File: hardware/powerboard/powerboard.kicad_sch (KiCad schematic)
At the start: 55 parts, among them J1 USB_B_Micro, J2 Boot Header, J3 Power Header, J4 SPI_0 Header, J5 Debug Header, J6 SPI_1 Header, J7 I2C_0 Header, J8 I2C_1 Header, SW1 Oct_Up, SW2 RESET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

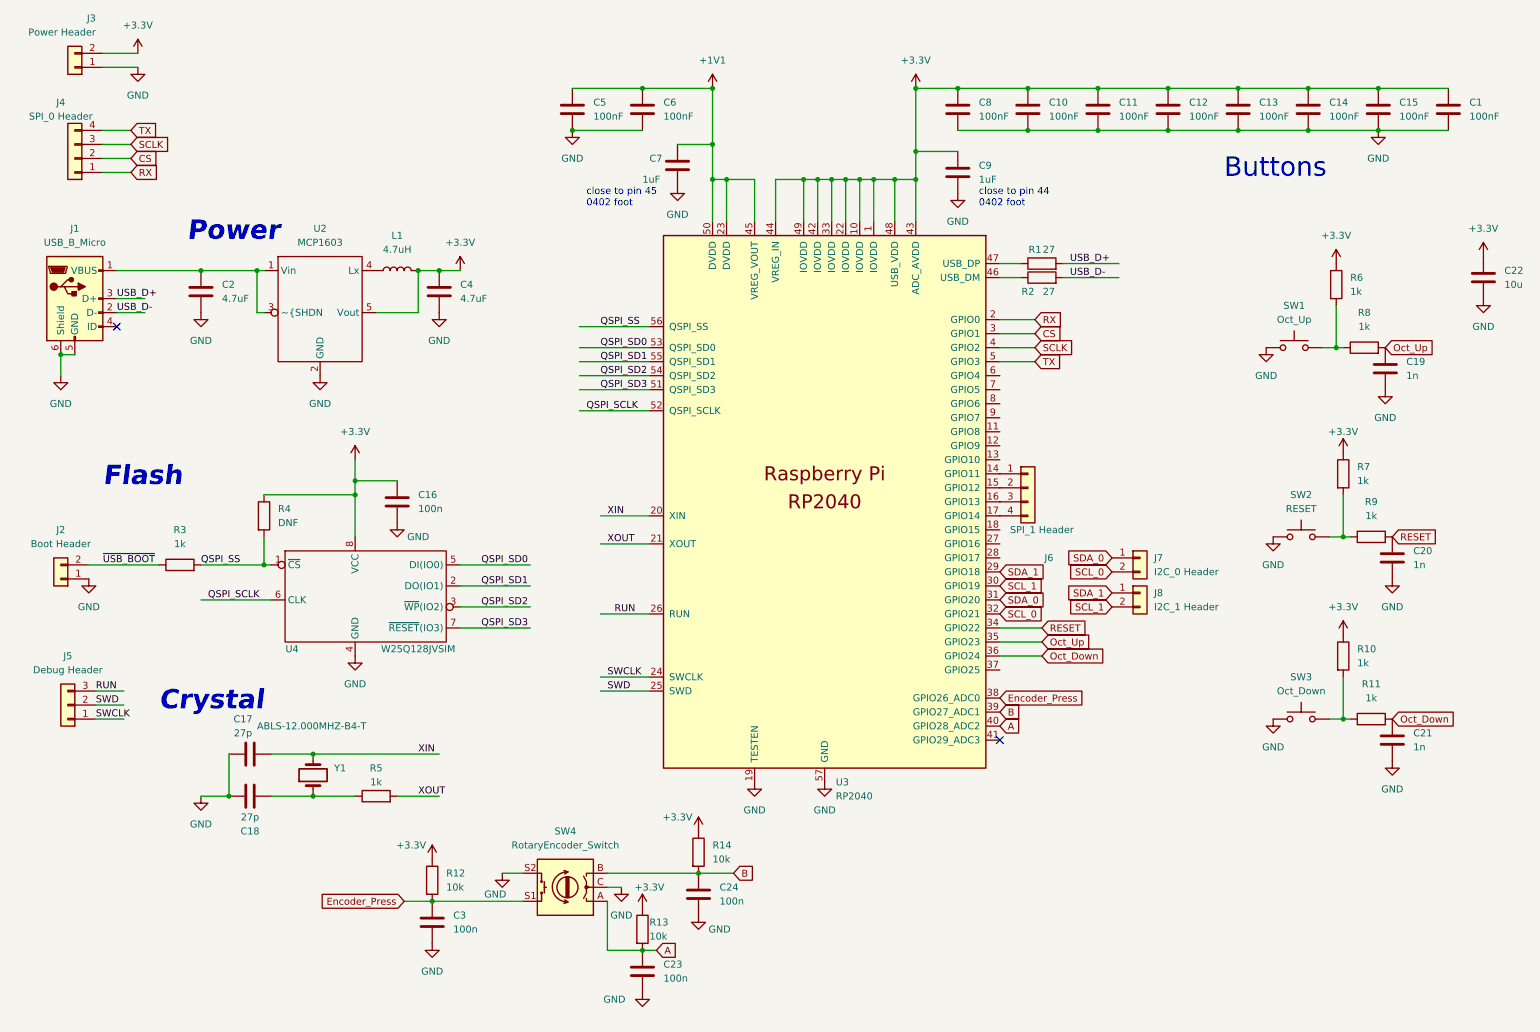
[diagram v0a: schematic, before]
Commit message: Power Board PCB: UART, LED's Smaller Crystal
Replaced Old Crystal with 3N12000G33YC
Added UART_0 with GP16 and GP17
Added 4 LED's with 330OHM Resistors on GP4-GP7
SPI Trace Widths 11.55 mil = 50Ohm Impedance
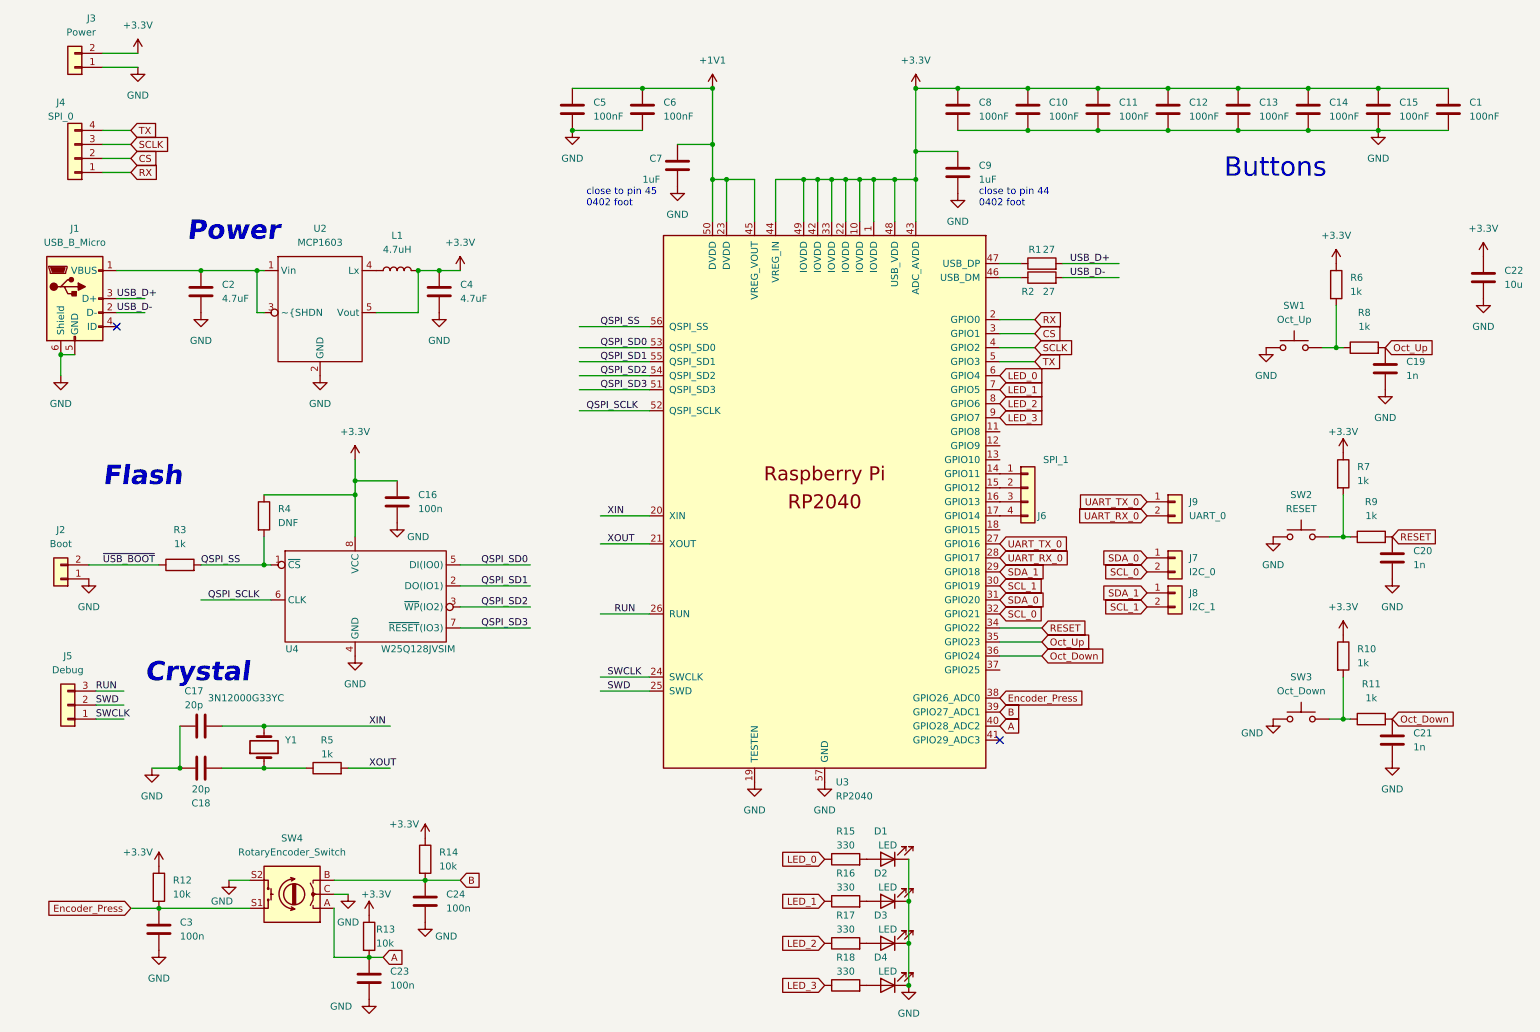
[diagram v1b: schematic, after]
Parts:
- added D1, D2, D3, D4: LED, LED_SMD:LED_0603_1608Metric, symbol Device:LED
- added J9: UART_0, Connector_PinHeader_2.54mm:PinHeader_1x02_P2.54mm_Vertical, symbol Connector_Generic:Conn_01x02
- added R15, R16, R17, R18: 330, Resistor_SMD:R_0603_1608Metric, symbol Device:R
- C17, C18: value 27p -> 20p
- J2: value Boot Header -> Boot
- J3: value Power Header -> Power
- J4: value SPI_0 Header -> SPI_0
- J5: value Debug Header -> Debug
- J6: value SPI_1 Header -> SPI_1
- J7: value I2C_0 Header -> I2C_0
- J8: value I2C_1 Header -> I2C_1
- Y1: value ABLS-12.000MHZ-B4-T -> 3N12000G33YC; footprint RP2040_minimal:Crystal_SMD_HC49-US -> Crystal:Crystal_SMD_3225-4Pin_3.2x2.5mm
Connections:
- net GND: now also D1.1 (K), D2.1 (K), D3.1 (K), D4.1 (K)
- net UART_TX_0: now reaches U3.27 (GPIO16)
- net UART_TX_0: now also J9.1 (Pin_1)
- net UART_RX_0: now reaches U3.28 (GPIO17)
- net UART_RX_0: now also J9.2 (Pin_2)
- net LED_0: now reaches U3.6 (GPIO4)
- net LED_0: now also R15.1
- net LED_1: now reaches U3.7 (GPIO5)
- net LED_1: now also R16.1
- net LED_2: now reaches U3.8 (GPIO6)
- net LED_2: now also R17.1
- net LED_3: now reaches U3.9 (GPIO7)
- net LED_3: now also R18.1
- new net: D4.2 (A), R18.2
- new net: D2.2 (A), R16.2
- new net: D3.2 (A), R17.2
- new net: D1.2 (A), R15.2
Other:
- moved on the sheet: C17, C18, C23, C24, C3, J7, J8, R12, R13, R14, R5, SW4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

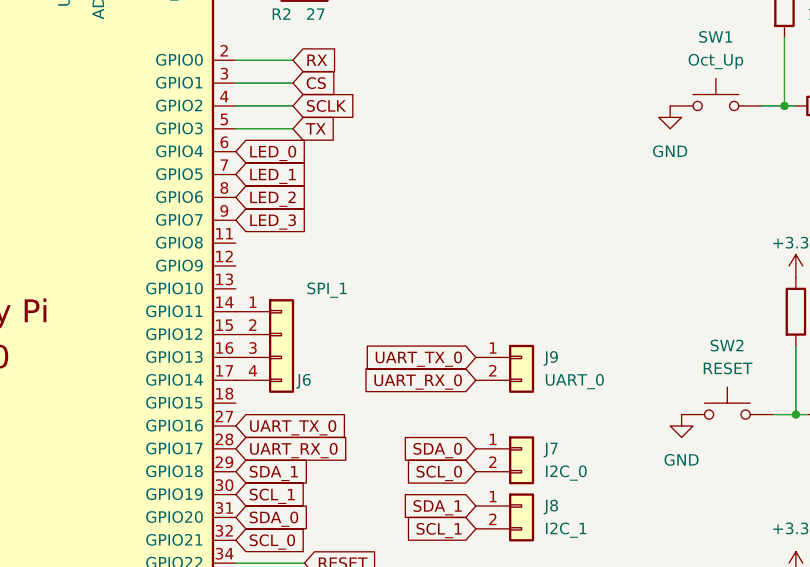
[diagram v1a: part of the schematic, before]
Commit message: Powerboard almsot done, need to finalize Power Circuit design
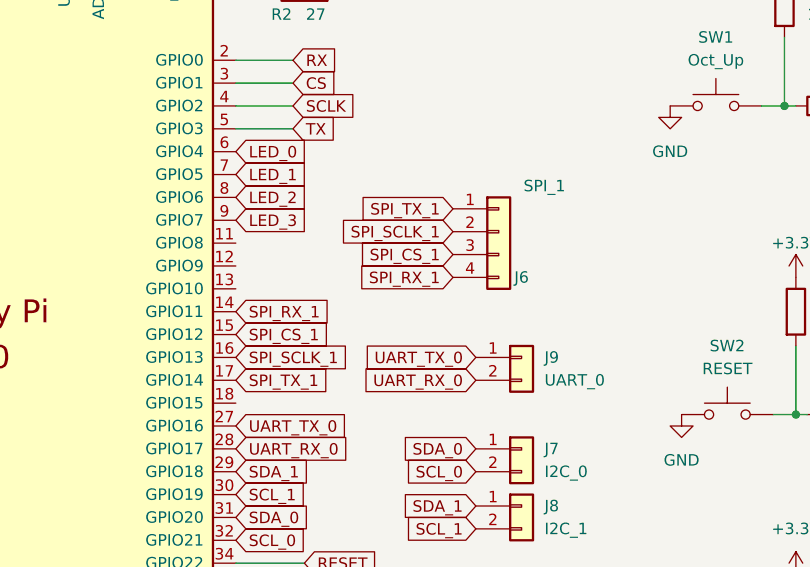
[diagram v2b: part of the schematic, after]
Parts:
- J3: footprint Connector_PinHeader_2.54mm:PinHeader_1x02_P2.54mm_Vertical -> Connector_PinHeader_2.54mm:PinHeader_1x02_P2.54mm_Horizontal
- J6: footprint Connector_PinHeader_2.54mm:PinHeader_1x04_P2.54mm_Vertical -> Connector_PinHeader_2.54mm:PinHeader_1x04_P2.54mm_Horizontal
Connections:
- net SPI_RX_1: now reaches U3.14 (GPIO11)
- net SPI_RX_1: now also J6.4 (Pin_4); no longer J6.1 (Pin_1)
- net SPI_CS_1: now reaches U3.15 (GPIO12)
- net SPI_CS_1: now also J6.3 (Pin_3); no longer J6.2 (Pin_2)
- net SPI_SCLK_1: now reaches U3.16 (GPIO13)
- net SPI_SCLK_1: now also J6.2 (Pin_2); no longer J6.3 (Pin_3)
- net SPI_TX_1: now reaches U3.17 (GPIO14)
- net SPI_TX_1: now also J6.1 (Pin_1); no longer J6.4 (Pin_4)
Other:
- moved on the sheet: J6
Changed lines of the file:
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@@
+    )
+  )
+  (global_label "SPI_SCLK_1" (shape input) (at 214.63 90.17 180) (fields_autoplaced)
+    (effects (font (size 1.27 1.27)) (justify right))
+    (property "Intersheet References" "${INTERSHEET_REFS}" (id 0) (at 201.2102 90.0906 0)
+      (effects (font (size 1.27 1.27)) (justify right) hide)
     )
   )
@@
     )
   )
+  (global_label "SPI_CS_1" (shape input) (at 214.63 92.71 180) (fields_autoplaced)
+    (effects (font (size 1.27 1.27)) (justify right))
+    (property "Intersheet References" "${INTERSHEET_REFS}" (id 0) (at 203.5083 92.6306 0)
+      (effects (font (size 1.27 1.27)) (justify right) hide)
+    )
+  )
   (global_label "RX" (shape input) (at 33.02 44.45 0) (fields_autoplaced)
     (effects (font (size 1.27 1.27)) (justify left))
@@
     )
   )
+  (global_label "SPI_SCLK_1" (shape input) (at 190.5 104.14 0) (fields_autoplaced)
+    (effects (font (size 1.27 1.27)) (justify left))
+    (property "Intersheet References" "${INTERSHEET_REFS}" (id 0) (at 203.9198 104.2194 0)
+      (effects (font (size 1.27 1.27)) (justify left) hide)
+    )
+  )
   (global_label "LED_1" (shape input) (at 158.75 176.53 180) (fields_autoplaced)
     (effects (font (size 1.27 1.27)) (justify right))
@@
     )
   )
+  (global_label "SPI_CS_1" (shape input) (at 190.5 101.6 0) (fields_autoplaced)
+    (effects (font (size 1.27 1.27)) (justify left))
+    (property "Intersheet References" "${INTERSHEET_REFS}" (id 0) (at 201.6217 101.6794 0)
+      (effects (font (size 1.27 1.27)) (justify left) hide)
+    )
+  )
   (global_label "SDA_0" (shape input) (at 190.5 121.92 0) (fields_autoplaced)
     (effects (font (size 1.27 1.27)) (justify left))
@@
     )
   )
+  (global_label "SPI_TX_1" (shape input) (at 214.63 87.63 180) (fields_autoplaced)
+    (effects (font (size 1.27 1.27)) (justify right))
+    (property "Intersheet References" "${INTERSHEET_REFS}" (id 0) (at 203.8107 87.5506 0)
+      (effects (font (size 1.27 1.27)) (justify right) hide)
+    )
+  )
   (global_label "TX" (shape input) (at 196.85 78.74 0) (fields_autoplaced)
     (effects (font (size 1.27 1.27)) (justify left))
@@
     (effects (font (size 1.27 1.27)) (justify left))
     (property "Intersheet References" "${INTERSHEET_REFS}" (id 0) (at 198.6583 116.7606 0)
+      (effects (font (size 1.27 1.27)) (justify left) hide)
+    )
+  )
+  (global_label "SPI_TX_1" (shape input) (at 190.5 106.68 0) (fields_autoplaced)
+    (effects (font (size 1.27 1.27)) (justify left))
+    (property "Intersheet References" "${INTERSHEET_REFS}" (id 0) (at 201.3193 106.7594 0)
       (effects (font (size 1.27 1.27)) (justify left) hide)
     )
@@
     )
   )
+  (global_label "SPI_RX_1" (shape input) (at 214.63 95.25 180) (fields_autoplaced)
+    (effects (font (size 1.27 1.27)) (justify right))
+    (property "Intersheet References" "${INTERSHEET_REFS}" (id 0) (at 203.5083 95.1706 0)
+      (effects (font (size 1.27 1.27)) (justify right) hide)
+    )
+  )
   (global_label "RESET" (shape input) (at 198.12 127 0) (fields_autoplaced)
     (effects (font (size 1.27 1.27)) (justify left))
     (property "Intersheet References" "${INTERSHEET_REFS}" (id 0) (at 206.2783 126.9206 0)
+      (effects (font (size 1.27 1.27)) (justify left) hide)
+    )
+  )
+  (global_label "SPI_RX_1" (shape input) (at 190.5 99.06 0) (fields_autoplaced)
+    (effects (font (size 1.27 1.27)) (justify left))
+    (property "Intersheet References" "${INTERSHEET_REFS}" (id 0) (at 201.6217 99.1394 0)
       (effects (font (size 1.27 1.27)) (justify left) hide)
     )
@@
       (effects (font (size 1.27 1.27)) (justify left))
     )
-    (property "Footprint" "Connector_PinHeader_2.54mm:PinHeader_1x02_P2.54mm_Vertical" (id 2) (at 22.86 25.4 0)
+    (property "Footprint" "Connector_PinHeader_2.54mm:PinHeader_1x02_P2.54mm_Horizontal" (id 2) (at 22.86 25.4 0)
       (effects (font (size 1.27 1.27)) hide)
     )
@@
     (pin "1")
   )
-  (symbol (lib_id "Connector_Generic:Conn_01x04") (at 195.58 101.6 0) (unit 1)
-    (in_bom yes) (on_board yes)
-    (property "Reference" "J6" (id 0) (at 198.12 106.68 0))
-    (property "Value" "SPI_1" (id 1) (at 200.66 96.52 0))
-    (property "Footprint" "Connector_PinHeader_2.54mm:PinHeader_1x04_P2.54mm_Vertical" (id 2) (at 195.58 101.6 0)
-      (effects (font (size 1.27 1.27)) hide)
-    )
-    (property "Datasheet" "~" (id 3) (at 195.58 101.6 0)
+  (symbol (lib_id "Connector_Generic:Conn_01x04") (at 219.71 90.17 0) (unit 1)
+    (in_bom yes) (on_board yes)
+    (property "Reference" "J6" (id 0) (at 222.25 95.25 0))
+    (property "Value" "SPI_1" (id 1) (at 224.79 85.09 0))
+    (property "Footprint" "Connector_PinHeader_2.54mm:PinHeader_1x04_P2.54mm_Horizontal" (id 2) (at 219.71 90.17 0)
+      (effects (font (size 1.27 1.27)) hide)
+    )
+    (property "Datasheet" "~" (id 3) (at 219.71 90.17 0)
       (effects (font (size 1.27 1.27)) hide)
     )
@@
     )
     (path "/425f7617-c8ff-4380-ba17-99301dfda302"
-      (reference "J3") (unit 1) (value "Power") (footprint "Connector_PinHeader_2.54mm:PinHeader_1x02_P2.54mm_Vertical")
+      (reference "J3") (unit 1) (value "Power") (footprint "Connector_PinHeader_2.54mm:PinHeader_1x02_P2.54mm_Horizontal")
     )
     (path "/f2b5b5c0-d4d9-43d2-86ba-dc803463a57e"
@@
     )
     (path "/e61389b3-9f11-48d3-8493-b121e9a672e9"
-      (reference "J6") (unit 1) (value "SPI_1") (footprint "Connector_PinHeader_2.54mm:PinHeader_1x04_P2.54mm_Vertical")
+      (reference "J6") (unit 1) (value "SPI_1") (footprint "Connector_PinHeader_2.54mm:PinHeader_1x04_P2.54mm_Horizontal")
     )
     (path "/65fec585-05a5-4019-84dd-a79686037b7c"
